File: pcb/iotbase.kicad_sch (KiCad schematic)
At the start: 37 parts, among them J1 USB_C_Receptacle_USB2.0, J2 RCWL-0516, J3 HSPI, J4 VSPI, SW1 Reset, SW2 Boot, U1 BME280, U2 AMS1117-3.3, U3 Connector_I2C, U4 Connector_I2C, U5 ESP32-WROOM-E, U6 Connector_IoT_GPIO, U7 Connector_ESProg, U8 HDC1080

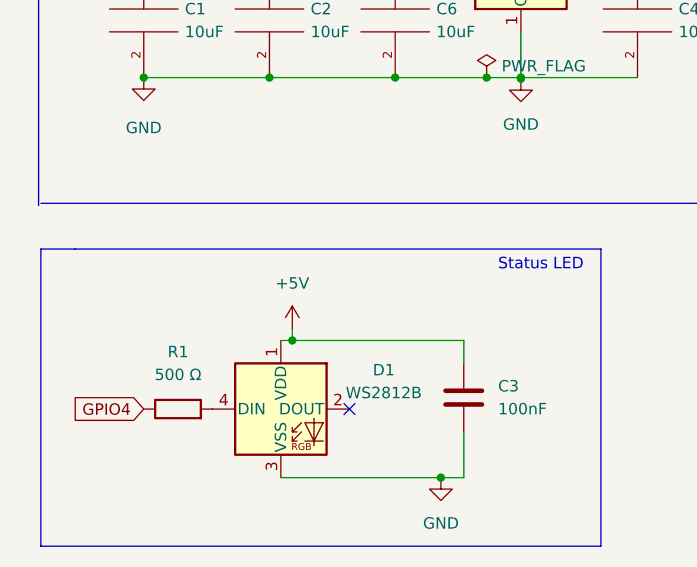
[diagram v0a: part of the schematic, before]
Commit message: connects WS2812 led to 3.3v, fixes #3
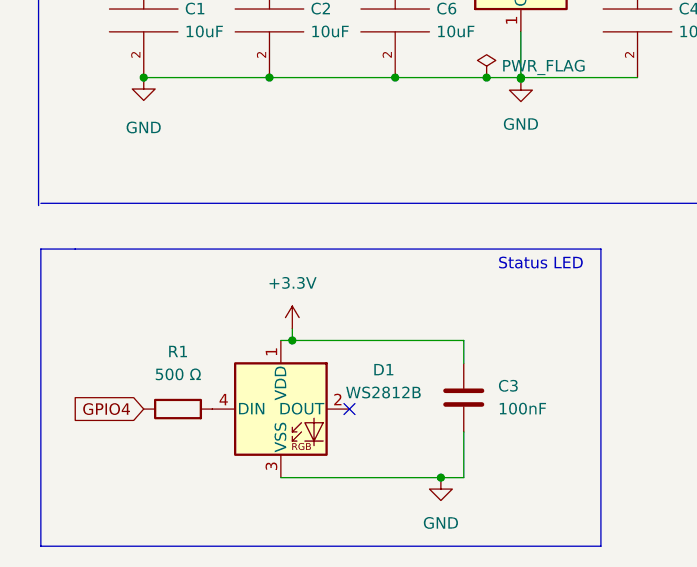
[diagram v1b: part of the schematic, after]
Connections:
- net +3V3: now also C3.1, D1.1 (VDD)
- net +5V: no longer C3.1, D1.1 (VDD)
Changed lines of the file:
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@@
+    (pin "1")
+  )
+  (symbol (lib_id "power:+3.3V") (at 57.15 132.08 0) (unit 1)
+    (in_bom yes) (on_board yes) (fields_autoplaced)
+    (property "Reference" "#PWR?" (id 0) (at 57.15 135.89 0)
+      (effects (font (size 1.27 1.27)) hide)
+    )
+    (property "Value" "+3.3V" (id 1) (at 57.15 127 0))
+    (property "Footprint" "" (id 2) (at 57.15 132.08 0)
+      (effects (font (size 1.27 1.27)) hide)
+    )
+    (property "Datasheet" "" (id 3) (at 57.15 132.08 0)
+      (effects (font (size 1.27 1.27)) hide)
+    )
     (pin "1")
   )
@@
     (pin "1")
   )
-  (symbol (lib_id "power:+5V") (at 57.15 132.08 0) (unit 1)
-    (in_bom yes) (on_board yes) (fields_autoplaced)
-    (property "Reference" "#PWR06" (id 0) (at 57.15 135.89 0)
-      (effects (font (size 1.27 1.27)) hide)
-    )
-    (property "Value" "+5V" (id 1) (at 57.15 127 0))
-    (property "Footprint" "" (id 2) (at 57.15 132.08 0)
-      (effects (font (size 1.27 1.27)) hide)
-    )
-    (property "Datasheet" "" (id 3) (at 57.15 132.08 0)
-      (effects (font (size 1.27 1.27)) hide)
-    )
-    (pin "1")
-  )
   (symbol (lib_id "power:GND") (at 82.55 104.267 0) (unit 1)
     (in_bom yes) (on_board yes) (fields_autoplaced)
@@
       (reference "#PWR05") (unit 1) (value "+3.3V") (footprint "")
     )
-    (path "/e3dea6dd-400d-415c-86a7-f39013f78a63"
-      (reference "#PWR06") (unit 1) (value "+5V") (footprint "")
-    )
     (path "/81a1f2cf-ee7f-48b7-8687-fba37e0af761"
       (reference "#PWR07") (unit 1) (value "GND") (footprint "")
@@
       (reference "#PWR0103") (unit 1) (value "GND") (footprint "")
     )
+    (path "/566f827a-7399-40f6-bf74-b7d9ef2f3204"
+      (reference "#PWR?") (unit 1) (value "+3.3V") (footprint "")
+    )
     (path "/801f7d23-296b-4c8c-8c1a-362b7cd0e7e8"

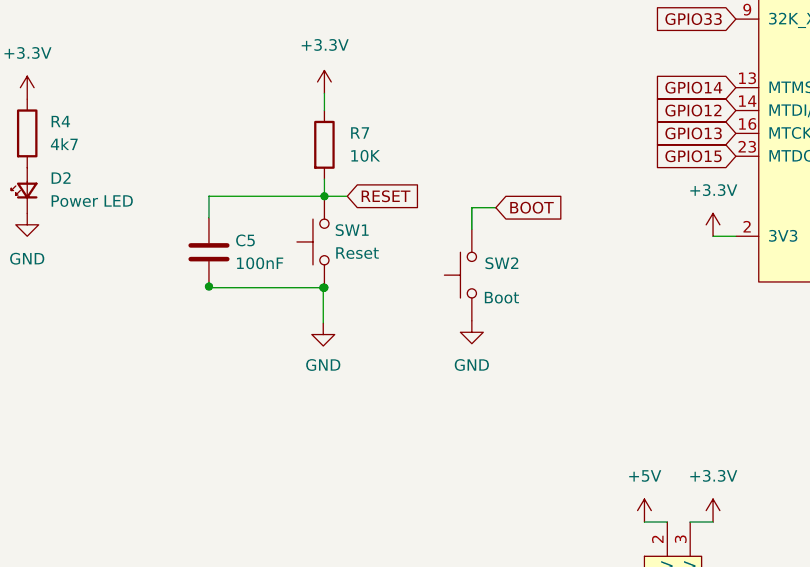
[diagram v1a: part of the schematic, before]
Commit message: fixes boot issues by updating C5 to 10uf
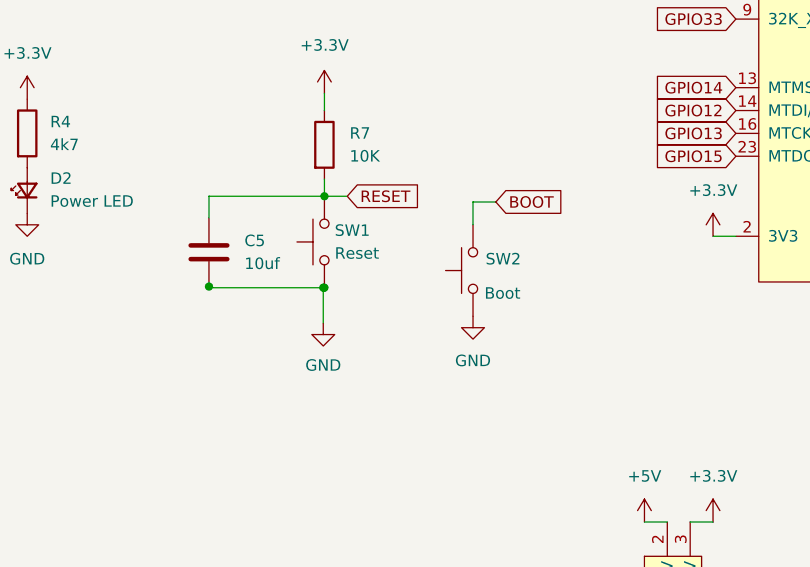
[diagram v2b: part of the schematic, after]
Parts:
- C5: value 100nF -> 10uf
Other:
- moved on the sheet: SW2
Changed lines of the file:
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@@
+    (stroke (width 0) (type default) (color 0 0 0 0))
+  )
+  (wire (pts (xy 170.18 93.98) (xy 172.72 93.98))
     (stroke (width 0) (type default) (color 0 0 0 0))
   )
@@
     (stroke (width 0) (type default) (color 0 0 0 0))
   )
+  (wire (pts (xy 170.18 93.98) (xy 170.18 96.52))
+    (stroke (width 0) (type default) (color 0 0 0 0))
+  )
   (wire (pts (xy 223.52 129.54) (xy 226.06 129.54))
     (stroke (width 0) (type default) (color 0 0 0 0))
@@
     (stroke (width 0) (type default) (color 0 0 0 0))
   )
-  (wire (pts (xy 170.053 94.615) (xy 170.053 97.028))
-    (stroke (width 0) (type default) (color 0 0 0 0))
-  )
   (polyline (pts (xy 29.21 123.19) (xy 33.02 123.19))
     (stroke (width 0) (type default) (color 0 0 0 0))
@@
   )
   (wire (pts (xy 142.24 186.69) (xy 146.05 186.69))
-    (stroke (width 0) (type default) (color 0 0 0 0))
-  )
-  (wire (pts (xy 172.72 94.615) (xy 170.053 94.615))
     (stroke (width 0) (type default) (color 0 0 0 0))
   )
@@
     )
   )
-  (global_label "BOOT" (shape input) (at 172.72 94.615 0) (fields_autoplaced)
+  (global_label "BOOT" (shape input) (at 172.72 93.98 0) (fields_autoplaced)
     (effects (font (size 1.27 1.27)) (justify left))
-    (property "Intersheet References" "${INTERSHEET_REFS}" (id 0) (at 180.0317 94.6944 0)
+    (property "Intersheet References" "${INTERSHEET_REFS}" (id 0) (at 180.0317 94.0594 0)
       (effects (font (size 1.27 1.27)) (justify left) hide)
     )
@@
     (pin "1")
   )
-  (symbol (lib_id "power:GND") (at 170.053 107.188 0) (unit 1)
-    (in_bom yes) (on_board yes) (fields_autoplaced)
-    (property "Reference" "#PWR018" (id 0) (at 170.053 113.538 0)
-      (effects (font (size 1.27 1.27)) hide)
-    )
-    (property "Value" "GND" (id 1) (at 170.053 112.141 0))
-    (property "Footprint" "" (id 2) (at 170.053 107.188 0)
-      (effects (font (size 1.27 1.27)) hide)
-    )
-    (property "Datasheet" "" (id 3) (at 170.053 107.188 0)
+  (symbol (lib_id "power:GND") (at 170.18 106.68 0) (unit 1)
+    (in_bom yes) (on_board yes) (fields_autoplaced)
+    (property "Reference" "#PWR018" (id 0) (at 170.18 113.03 0)
+      (effects (font (size 1.27 1.27)) hide)
+    )
+    (property "Value" "GND" (id 1) (at 170.18 111.633 0))
+    (property "Footprint" "" (id 2) (at 170.18 106.68 0)
+      (effects (font (size 1.27 1.27)) hide)
+    )
+    (property "Datasheet" "" (id 3) (at 170.18 106.68 0)
       (effects (font (size 1.27 1.27)) hide)
     )
@@
   (symbol (lib_id "power:+3.3V") (at 57.15 132.08 0) (unit 1)
     (in_bom yes) (on_board yes) (fields_autoplaced)
-    (property "Reference" "#PWR?" (id 0) (at 57.15 135.89 0)
+    (property "Reference" "#PWR0104" (id 0) (at 57.15 135.89 0)
       (effects (font (size 1.27 1.27)) hide)
     )
@@
     (pin "1")
   )
-  (symbol (lib_id "Switch:SW_Push") (at 170.053 102.108 90) (unit 1)
+  (symbol (lib_id "Switch:SW_Push") (at 170.18 101.6 90) (unit 1)
     (in_bom yes) (on_board yes)
-    (property "Reference" "SW2" (id 0) (at 171.45 100.8379 90)
+    (property "Reference" "SW2" (id 0) (at 171.577 100.3299 90)
       (effects (font (size 1.27 1.27)) (justify right))
     )
-    (property "Value" "Boot" (id 1) (at 171.323 104.648 90)
+    (property "Value" "Boot" (id 1) (at 171.45 104.14 90)
       (effects (font (size 1.27 1.27)) (justify right))
     )
-    (property "Footprint" "Button_Switch_SMD:SW_SPST_CK_RS282G05A3" (id 2) (at 164.973 102.108 0)
-      (effects (font (size 1.27 1.27)) hide)
-    )
-    (property "Datasheet" "~" (id 3) (at 164.973 102.108 0)
-      (effects (font (size 1.27 1.27)) hide)
-    )
-    (property "LSCID" "C118141" (id 5) (at 170.053 102.108 0)
+    (property "Footprint" "Button_Switch_SMD:SW_SPST_CK_RS282G05A3" (id 2) (at 165.1 101.6 0)
+      (effects (font (size 1.27 1.27)) hide)
+    )
+    (property "Datasheet" "~" (id 3) (at 165.1 101.6 0)
+      (effects (font (size 1.27 1.27)) hide)
+    )
+    (property "LSCID" "C118141" (id 5) (at 170.18 101.6 0)
       (effects (font (size 1.27 1.27)) hide)
     )
@@
   (symbol (lib_id "Device:C") (at 140.843 99.568 0) (unit 1)
     (in_bom yes) (on_board yes) (fields_autoplaced)
-    (property "Reference" "C5" (id 0) (at 143.764 98.2979 0)
-      (effects (font (size 1.27 1.27)) (justify left))
-    )
-    (property "Value" "100nF" (id 1) (at 143.764 100.8379 0)
+    (property "Reference" "C5" (id 0) (at 144.78 98.2979 0)
+      (effects (font (size 1.27 1.27)) (justify left))
+    )
+    (property "Value" "10uf" (id 1) (at 144.78 100.8379 0)
       (effects (font (size 1.27 1.27)) (justify left))
     )
@@
     )
     (path "/566f827a-7399-40f6-bf74-b7d9ef2f3204"
-      (reference "#PWR?") (unit 1) (value "+3.3V") (footprint "")
+      (reference "#PWR0104") (unit 1) (value "+3.3V") (footprint "")
     )
     (path "/801f7d23-296b-4c8c-8c1a-362b7cd0e7e8"
@@
     )
     (path "/d4604b74-66e3-49de-99f5-6d9bdf91def6"
-      (reference "C5") (unit 1) (value "100nF") (footprint "Capacitor_SMD:C_0603_1608Metric")
+      (reference "C5") (unit 1) (value "10uf") (footprint "Capacitor_SMD:C_0603_1608Metric")
     )
     (path "/993be68a-612a-4351-9c9e-d11117cdf80a"

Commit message: reduced pcb size added header for RCWL-0516 removed BME280 to save on cost replaced buttons with solder pads
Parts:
- removed CB1, CB2: 100nF, Capacitor_SMD:C_0603_1608Metric, symbol Device:C
- removed J2: RCWL-0516, 0_Project:PinHeader_RCWL-0516, symbol Connector_Generic:Conn_01x05
- removed SW1: Reset, Button_Switch_SMD:SW_SPST_CK_RS282G05A3, symbol Switch:SW_Push
- removed SW2: Boot, Button_Switch_SMD:SW_SPST_CK_RS282G05A3, symbol Switch:SW_Push
- removed U1: BME280, Package_LGA:Bosch_LGA-8_2.5x2.5mm_P0.65mm_ClockwisePinNumbering, symbol Sensor:BME280
- added C7, C8: 1000uf, Capacitor_SMD:C_0603_1608Metric, symbol Device:C
- added J2: RCWL-0516, Connector_PinHeader_2.54mm:PinHeader_1x03_P2.54mm_Vertical, symbol Connector_Generic:Conn_01x03
- added JP1: Reset, Jumper:SolderJumper-2_P1.3mm_Open_RoundedPad1.0x1.5mm, symbol Jumper:SolderJumper_2_Open
- added JP2: Boot, Jumper:SolderJumper-2_P1.3mm_Open_RoundedPad1.0x1.5mm, symbol Jumper:SolderJumper_2_Open
- added R7: 10Ω, Resistor_SMD:R_0603_1608Metric, symbol Device:R
- added R9: 10K, Resistor_SMD:R_0603_1608Metric, symbol Device:R
- renumbered C6 to C3, C3 to C4, C4 to C5, C5 to C6, RB2 to R10, RB1 to R11, R5 to R4, R6 to R5, R4 to R6, R7 to R8, U8 to U1
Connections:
- net +5V: now also C7.1, R7.1
- net BOOT: now also JP2.2 (B)
- net GND: now also C7.2, C8.2, J2.3 (Pin_3), JP1.1 (A), JP2.1 (A), R9.2
- net GPIO16: now also R1.1; no longer U6.14 (GPIO16)
- net GPIO4: now also U6.14 (GPIO16); no longer R1.1
- net IO36: now also J2.2 (Pin_2), R9.1
- net RESET: now also JP1.2 (B)
- new net: C8.1, J2.1 (Pin_1), R7.2
- no-connect marks 11 -> 9
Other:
- note added: "Temp/Humidity Sensor HDC1080"
- note removed: "BME280 Temperature & Humidity Sensor"
- moved on the sheet: C6, R10, R11, R4, R5, R8, U1

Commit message: updates jlcpcb compoent id's
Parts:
- C6: value 10uf -> 10uF
- C7, C8: value 1000uf -> 1000uF
- J2, JP1, JP2: now left out of the parts list
- R10, R11: value 4.7 K -> 4.7 KΩ
- R2, R3, R6: value 4k7 -> 4.7 KΩ
- R8, R9: value 10K -> 10kΩ
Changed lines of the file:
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@@
   (symbol (lib_id "Device:R") (at 302.26 64.77 180) (unit 1)
     (in_bom yes) (on_board yes) (fields_autoplaced)
-    (property "Reference" "R10" (id 0) (at 299.72 66.0401 0)
-      (effects (font (size 1.27 1.27)) (justify left))
-    )
-    (property "Value" "4.7 K" (id 1) (at 299.72 63.5001 0)
-      (effects (font (size 1.27 1.27)) (justify left))
+    (property "Reference" "R10" (id 0) (at 304.8 63.4999 0)
+      (effects (font (size 1.27 1.27)) (justify right))
+    )
+    (property "Value" "4.7 KΩ" (id 1) (at 304.8 66.0399 0)
+      (effects (font (size 1.27 1.27)) (justify right))
     )
     (property "Footprint" "Resistor_SMD:R_0603_1608Metric" (id 2) (at 304.038 64.77 90)
@@
   )
   (symbol (lib_id "Jumper:SolderJumper_2_Open") (at 170.18 100.33 90) (unit 1)
-    (in_bom yes) (on_board yes) (fields_autoplaced)
+    (in_bom no) (on_board yes) (fields_autoplaced)
     (property "Reference" "JP2" (id 0) (at 172.72 99.0599 90)
       (effects (font (size 1.27 1.27)) (justify right))
@@
     (in_bom yes) (on_board yes)
     (property "Reference" "R3" (id 0) (at 76.2 38.1 90))
-    (property "Value" "4k7" (id 1) (at 76.2 40.894 90))
+    (property "Value" "4.7 KΩ" (id 1) (at 76.2 40.894 90))
     (property "Footprint" "Resistor_SMD:R_0603_1608Metric" (id 2) (at 76.2 39.878 90)
       (effects (font (size 1.27 1.27)) hide)
@@
   (symbol (lib_id "Device:R") (at 152.4 87.63 0) (unit 1)
     (in_bom yes) (on_board yes) (fields_autoplaced)
-    (property "Reference" "R8" (id 0) (at 155.194 86.3599 0)
-      (effects (font (size 1.27 1.27)) (justify left))
-    )
-    (property "Value" "10K" (id 1) (at 155.194 88.8999 0)
+    (property "Reference" "R8" (id 0) (at 154.94 86.3599 0)
+      (effects (font (size 1.27 1.27)) (justify left))
+    )
+    (property "Value" "10kΩ" (id 1) (at 154.94 88.8999 0)
       (effects (font (size 1.27 1.27)) (justify left))
     )
@@
       (effects (font (size 1.27 1.27)) (justify left))
     )
-    (property "Value" "1000uf" (id 1) (at 158.75 185.42 0)
+    (property "Value" "1000uF" (id 1) (at 158.75 185.42 0)
       (effects (font (size 1.27 1.27)) (justify left))
     )
@@
       (effects (font (size 1.27 1.27)) (justify left))
     )
-    (property "Value" "1000uf" (id 1) (at 144.78 185.4199 0)
+    (property "Value" "1000uF" (id 1) (at 144.78 185.4199 0)
       (effects (font (size 1.27 1.27)) (justify left))
     )
@@
       (effects (font (size 1.27 1.27)) (justify right))
     )
-    (property "Value" "4.7 K" (id 1) (at 314.96 66.0399 0)
+    (property "Value" "4.7 KΩ" (id 1) (at 314.96 66.0399 0)
       (effects (font (size 1.27 1.27)) (justify right))
     )
@@
   )
   (symbol (lib_id "Jumper:SolderJumper_2_Open") (at 152.4 97.79 90) (unit 1)
-    (in_bom yes) (on_board yes) (fields_autoplaced)
+    (in_bom no) (on_board yes) (fields_autoplaced)
     (property "Reference" "JP1" (id 0) (at 154.94 96.5199 90)
       (effects (font (size 1.27 1.27)) (justify right))
@@
       (effects (font (size 1.27 1.27)) (justify left))
     )
-    (property "Value" "10K" (id 1) (at 174.244 186.6899 0)
+    (property "Value" "10kΩ" (id 1) (at 174.244 186.6899 0)
       (effects (font (size 1.27 1.27)) (justify left))
     )
@@
     (in_bom yes) (on_board yes)
     (property "Reference" "R2" (id 0) (at 76.2 33.02 90))
-    (property "Value" "4k7" (id 1) (at 76.2 35.56 90))
+    (property "Value" "4.7 KΩ" (id 1) (at 76.2 35.56 90))
     (property "Footprint" "Resistor_SMD:R_0603_1608Metric" (id 2) (at 76.2 34.798 90)
       (effects (font (size 1.27 1.27)) hide)
@@
       (effects (font (size 1.27 1.27)) (justify left))
     )
-    (property "Value" "4k7" (id 1) (at 123.19 87.6299 0)
+    (property "Value" "4.7 KΩ" (id 1) (at 123.19 87.6299 0)
       (effects (font (size 1.27 1.27)) (justify left))
     )
@@
       (effects (font (size 1.27 1.27)) (justify left))
     )
-    (property "Value" "10uf" (id 1) (at 143.51 100.8379 0)
+    (property "Value" "10uF" (id 1) (at 143.51 100.8379 0)
       (effects (font (size 1.27 1.27)) (justify left))
     )
@@
   )
   (symbol (lib_id "Connector_Generic:Conn_01x03") (at 184.15 181.61 0) (unit 1)
-    (in_bom yes) (on_board yes) (fields_autoplaced)
+    (in_bom no) (on_board yes) (fields_autoplaced)
     (property "Reference" "J2" (id 0) (at 186.69 180.3399 0)
       (effects (font (size 1.27 1.27)) (justify left))
@@
     )
     (path "/d4604b74-66e3-49de-99f5-6d9bdf91def6"
-      (reference "C6") (unit 1) (value "10uf") (footprint "Capacitor_SMD:C_0603_1608Metric")
+      (reference "C6") (unit 1) (value "10uF") (footprint "Capacitor_SMD:C_0603_1608Metric")
     )
     (path "/68a3be16-f414-4e2c-8f32-5a7fd6cba677"
-      (reference "C7") (unit 1) (value "1000uf") (footprint "Capacitor_SMD:C_0603_1608Metric")
+      (reference "C7") (unit 1) (value "1000uF") (footprint "Capacitor_SMD:C_0603_1608Metric")
     )
     (path "/60c2f028-f74d-437f-bd00-2ef08aaa39c8"
-      (reference "C8") (unit 1) (value "1000uf") (footprint "Capacitor_SMD:C_0603_1608Metric")
+      (reference "C8") (unit 1) (value "1000uF") (footprint "Capacitor_SMD:C_0603_1608Metric")
     )
     (path "/5d7cb436-106e-4464-b448-3b8bd128554c"
@@
     )
     (path "/9107f90e-86a8-40ce-9b18-211cf27a70d8"
-      (reference "R2") (unit 1) (value "4k7") (footprint "Resistor_SMD:R_0603_1608Metric")
+      (reference "R2") (unit 1) (value "4.7 KΩ") (footprint "Resistor_SMD:R_0603_1608Metric")
     )
     (path "/31241600-8786-4da7-9e3e-b0abbfafc490"
-      (reference "R3") (unit 1) (value "4k7") (footprint "Resistor_SMD:R_0603_1608Metric")
+      (reference "R3") (unit 1) (value "4.7 KΩ") (footprint "Resistor_SMD:R_0603_1608Metric")
     )
     (path "/6d1123a2-0576-4892-869b-cba83a733037"
@@
     )
     (path "/c23806e2-2103-4b84-9d48-a8f7045018f0"
-      (reference "R6") (unit 1) (value "4k7") (footprint "Resistor_SMD:R_0603_1608Metric")
+      (reference "R6") (unit 1) (value "4.7 KΩ") (footprint "Resistor_SMD:R_0603_1608Metric")
     )
     (path "/e1cf9b8f-034a-41d3-9d3f-11035a8c7fa8"
@@
     )
     (path "/5ba637a8-7ecb-45f0-a9f3-674db32e1151"
-      (reference "R8") (unit 1) (value "10K") (footprint "Resistor_SMD:R_0603_1608Metric")
+      (reference "R8") (unit 1) (value "10kΩ") (footprint "Resistor_SMD:R_0603_1608Metric")
     )
     (path "/830f6e69-0557-4500-9cfa-ade38dca65e7"
-      (reference "R9") (unit 1) (value "10K") (footprint "Resistor_SMD:R_0603_1608Metric")
+      (reference "R9") (unit 1) (value "10kΩ") (footprint "Resistor_SMD:R_0603_1608Metric")
     )
     (path "/128a7556-cb3d-406d-b84d-6d9efc7f9ed8"
-      (reference "R10") (unit 1) (value "4.7 K") (footprint "Resistor_SMD:R_0603_1608Metric")
+      (reference "R10") (unit 1) (value "4.7 KΩ") (footprint "Resistor_SMD:R_0603_1608Metric")
     )
     (path "/73fd78b9-9aa5-40d0-adab-1e5886c90dd7"
-      (reference "R11") (unit 1) (value "4.7 K") (footprint "Resistor_SMD:R_0603_1608Metric")
+      (reference "R11") (unit 1) (value "4.7 KΩ") (footprint "Resistor_SMD:R_0603_1608Metric")
     )
     (path "/1f733bbe-7d73-46c8-b4ea-2ccc6df76ebe"

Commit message: release rev. 0.2
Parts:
- removed C7, C8: 1000uF, Capacitor_SMD:C_0603_1608Metric, symbol Device:C
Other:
- note added: ""Buttons""
- note added: "GPIO Header"
- note added: "I2C Header"
- note added: "Mounting Holes"
- note added: "Power LED"
- note added: "Programming Header"
- note added: "SPI Header"
- moved on the sheet: C6, D2, H1, H2, H3, H4, J2, J3, J4, JP1, JP2, R10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
